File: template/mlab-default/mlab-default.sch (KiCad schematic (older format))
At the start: 8 parts, among them J1 Umin ... Umax, M1 HOLE, M2 HOLE, M3 HOLE, M4 HOLE

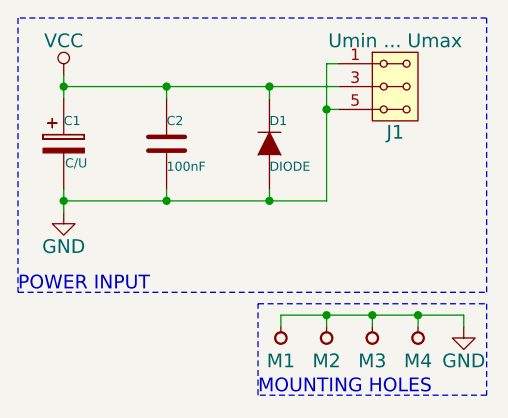
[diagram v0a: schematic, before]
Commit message: Changed to meet the new Mlab standards
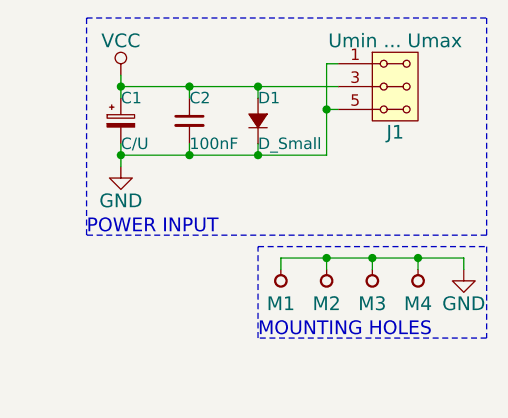
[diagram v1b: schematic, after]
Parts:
- removed C1: C/U, symbol CP2
- removed C2: 100nF, symbol C
- removed D1: DIODE, symbol DIODE
- added C1: C/U, symbol CP_Small
- added C2: 100nF, symbol C_Small
- added D1: D_Small, symbol D_Small
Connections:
- net GND: now also C1.2, C2.2, D1.1 (K)
- net VCC: now also C1.1, C2.1, D1.2 (A)
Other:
- moved on the sheet: M1, M2, M3, M4
